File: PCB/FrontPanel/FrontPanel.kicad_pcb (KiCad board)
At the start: 2 copper layers, 130.8 x 44.5 mm, 52 parts, among them J1 Conn_01x05, J2 Conn_01x03, Q1 2N7002, Q2 2N7002, Q3 2N7002, Q4 2N7002, Q5 2N7002, SW1 SW_SPDT, SW10 RArrow, SW2 RotaryEncoder_Switch, SW3 IndepChSelect, SW4 SeriesChSelect, SW5 ParChSelect, SW6 ChAEnable, SW7 ChBEnable, SW8 ABSelect, SW9 LArrow, U1 MCU_ST_STM32G0:STM32G031F6Px, U2 CD74HC4067SM

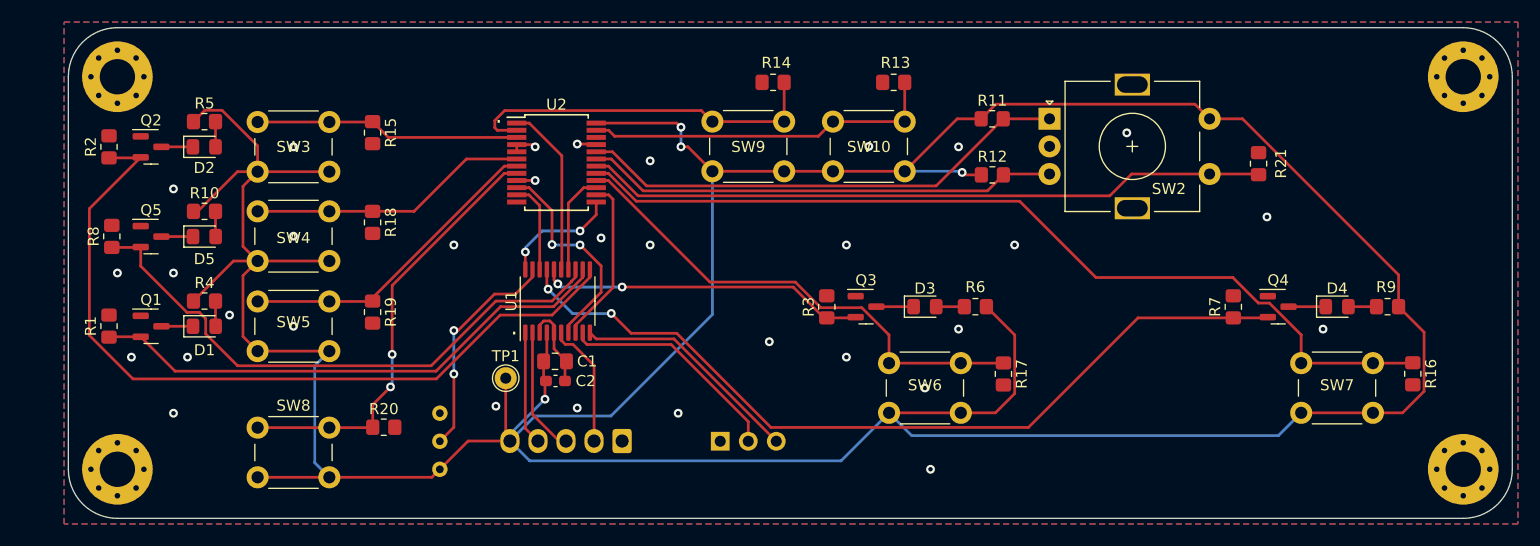
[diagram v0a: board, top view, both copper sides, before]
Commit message: Add SWD connector
USART programming is fraught with problems. It's much much
better to use SWD through an STDC14 connector.
Increased version number to v1.3
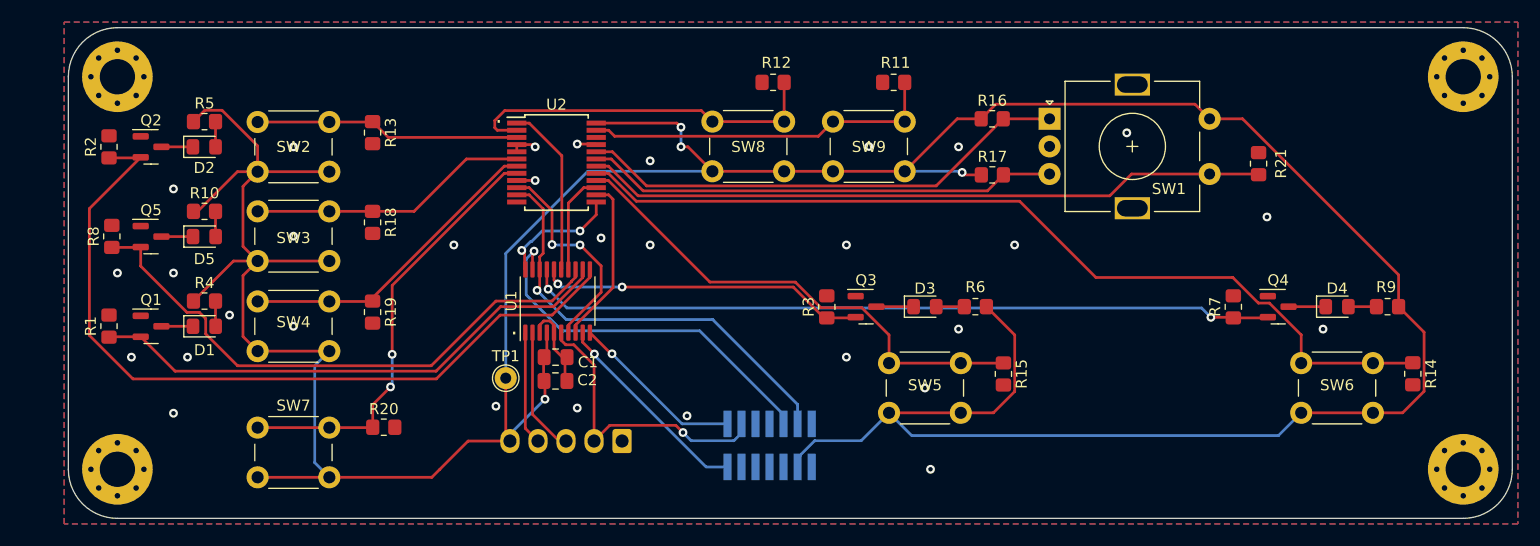
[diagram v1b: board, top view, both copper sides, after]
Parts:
- removed the SW1 at (158.8, 76.2)
- C2: footprint Capacitor_SMD:C_0603_1608Metric_Pad1.08x0.95mm_HandSolder -> Capacitor_SMD:C_0805_2012Metric_Pad1.18x1.45mm_HandSolder
- J2: value Conn_01x03 -> SWD; footprint Connector_PinHeader_2.54mm:PinHeader_1x03_P2.54mm_Vertical -> Connector_PinHeader_1.27mm:PinHeader_2x07_P1.27mm_Vertical_SMD
- moved J2 4.49 mm to (188.6, 76.6), turned to 90 degrees
- moved C1 0.38 mm to (169.2, 68.6)
- renumbered R13 to R11, R14 to R12, R15 to R13, R16 to R14, R17 to R15, R11 to R16, R12 to R17, SW2 to SW1, SW3 to SW2, SW4 to SW3, SW5 to SW4, SW6 to SW5, SW7 to SW6, SW8 to SW7, SW9 to SW8, SW10 to SW9
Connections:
- J2 pad 1: GND -> unconnected-(J2-Pad1)
- J2 pad 2: UART_TX -> unconnected-(J2-Pad2)
- J2 pad 3: UART_RX -> VCC
- U1 pad 18: S1 -> SWDIO/S1
- U1 pad 19: BOOT0 -> SWCLK
- U2 pad 11: S1 -> SWDIO/S1
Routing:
- net SWDIO/S1: track 0.00 -> 40.2 mm, vias 0 -> 1
- net SWCLK: track 0.00 -> 34.7 mm, vias 0 -> 1
- net VCC: track 364.5 -> 335.3 mm
- net BOOT0: track 20.4 -> 0.00 mm, vias 2 -> 0
- net NRESET: track 11.5 -> 27.1 mm, vias 0 -> 1
- net S1: track 8.26 -> 0.00 mm
- net CHANNEL_B_EN: track 76.4 -> 68.1 mm
- net UART_RX: track 21.0 -> 15.9 mm, vias 0 -> 1
- net UART_TX: track 20.5 -> 18.7 mm, vias 0 -> 1
- net GND: vias 32 -> 31
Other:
- board text added: "FW programming SWD interface"
- board text added: "Font del Gat Front Panel PCB v1.3 by Pau Estalella"
- board text removed: "FW programming UART interface"
- board text removed: "Font del Gat Front Panel PCB v1.2 by Pau Estalella"
- board text removed: "RX"
- board text removed: "TX"

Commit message: Give names to all networks a name
Add network labels to networks that didn't yet have a name.
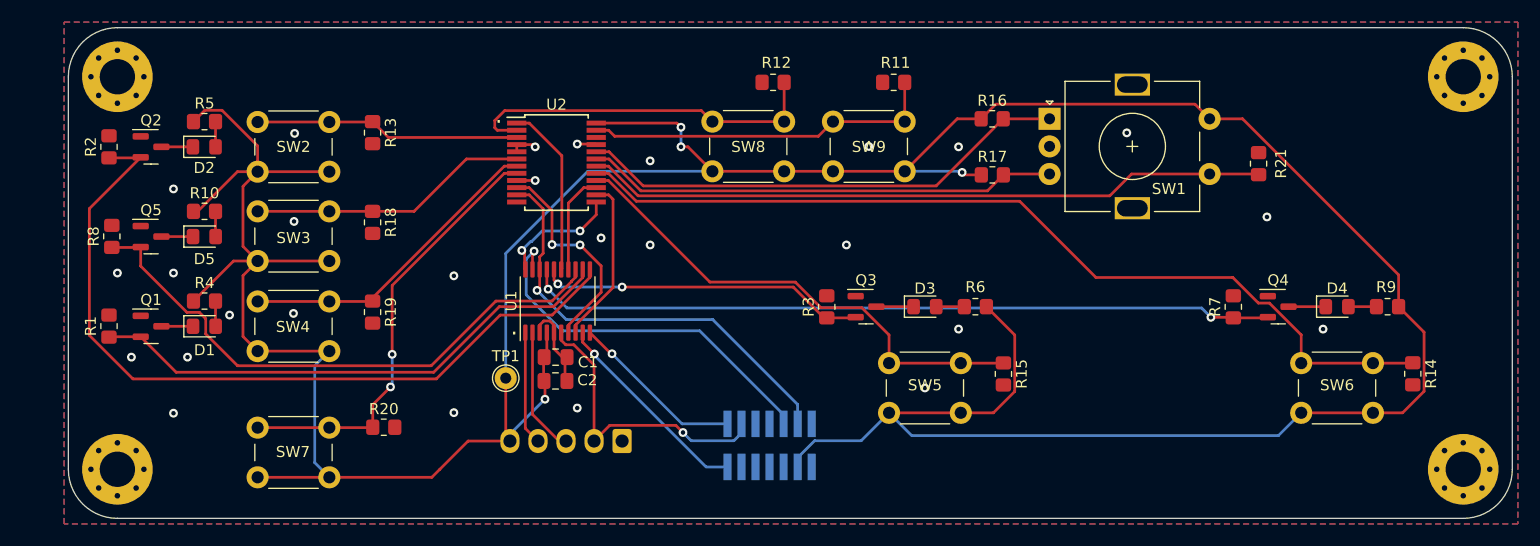
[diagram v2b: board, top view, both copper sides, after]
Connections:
- net Net-(R11-Pad1) renamed /RArrowSw
- net Net-(R12-Pad1) renamed /LArrowSw
- net Net-(R13-Pad1) renamed /IndepSelectSw
- net Net-(R14-Pad1) renamed /ChBEnableSw
- net Net-(R15-Pad1) renamed /ChAEnableSw
- net Net-(R18-Pad1) renamed /SeriesSelectSw
- net Net-(R19-Pad1) renamed /ParSelectSw
- net Net-(R20-Pad1) renamed /ABSelectSw
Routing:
- net GND: vias 31 -> 27
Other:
- board text removed: "BOOTP"
- board text removed: "USER"

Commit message: Fix 2N7002 footprint
The footprint for the 2N7002 MOSFETs was taken from the one
of a 2N7000, which has the gate and the source pins exchanged.
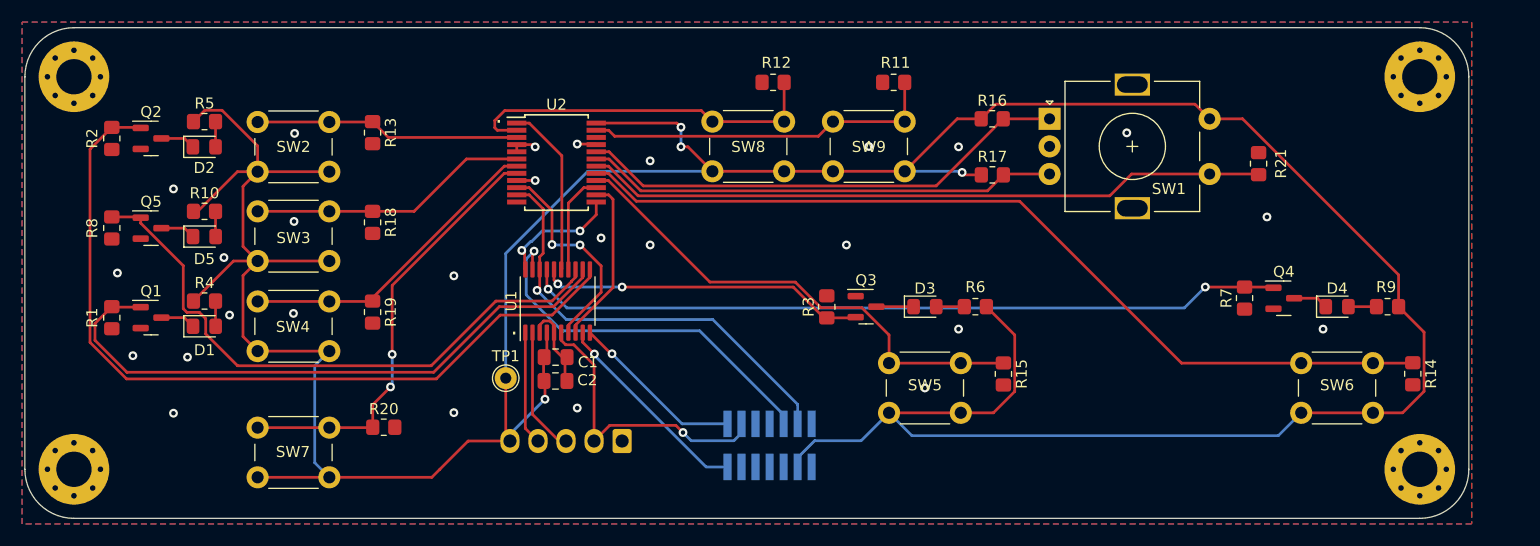
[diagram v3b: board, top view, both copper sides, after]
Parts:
- moved H2 3.94 mm to (247.5, 43.2)
- moved H4 3.94 mm to (247.5, 78.7)
- moved H1 3.94 mm to (125.6, 78.7)
- moved H3 3.94 mm to (125.6, 43.2)
- moved R7 1.29 mm to (231.6, 63.2), turned to -90 degrees
- moved Q4 0.92 mm to (235.2, 63.2)
- moved R1 0.80 mm to (129.0, 65.0), turned to -90 degrees
- moved R2 0.80 mm to (129.0, 48.8), turned to -90 degrees
- moved Q1 0.79 mm to (132.6, 65.0)
- moved Q2 0.76 mm to (132.6, 48.8)
- moved Q5 0.76 mm to (132.6, 56.9)
- moved R8 0.76 mm to (129.0, 56.9), turned to -90 degrees
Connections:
- Q1 pad 1: GND -> PAR_CHANNEL_EN
- Q1 pad 2: PAR_CHANNEL_EN -> GND
- Q2 pad 1: GND -> INDEP_CHANNEL_EN
- Q2 pad 2: INDEP_CHANNEL_EN -> GND
- Q4 pad 1: GND -> CHANNEL_B_EN
- Q4 pad 2: CHANNEL_B_EN -> GND
- Q5 pad 1: GND -> SERIES_CHANNEL_EN
- Q5 pad 2: SERIES_CHANNEL_EN -> GND
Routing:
- net PAR_CHANNEL_EN: track 48.5 -> 56.0 mm
- net SERIES_CHANNEL_EN: track 52.3 -> 55.0 mm
- net INDEP_CHANNEL_EN: track 72.4 -> 74.1 mm
- net /ChBEnableSw: track 82.6 -> 81.1 mm
- net CHANNEL_B_EN: track 68.1 -> 69.1 mm
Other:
- board text added: "Font del Gat Front Panel PCB v1.4 by Pau Estalella"
- board text removed: "Font del Gat Front Panel PCB v1.3 by Pau Estalella"

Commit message: Fixes for the front panel
Add a 3V3 regulator to convert the 5V input.
Fix RX/TX mix-up
Fix footprint for one last 2N7002 mosfet
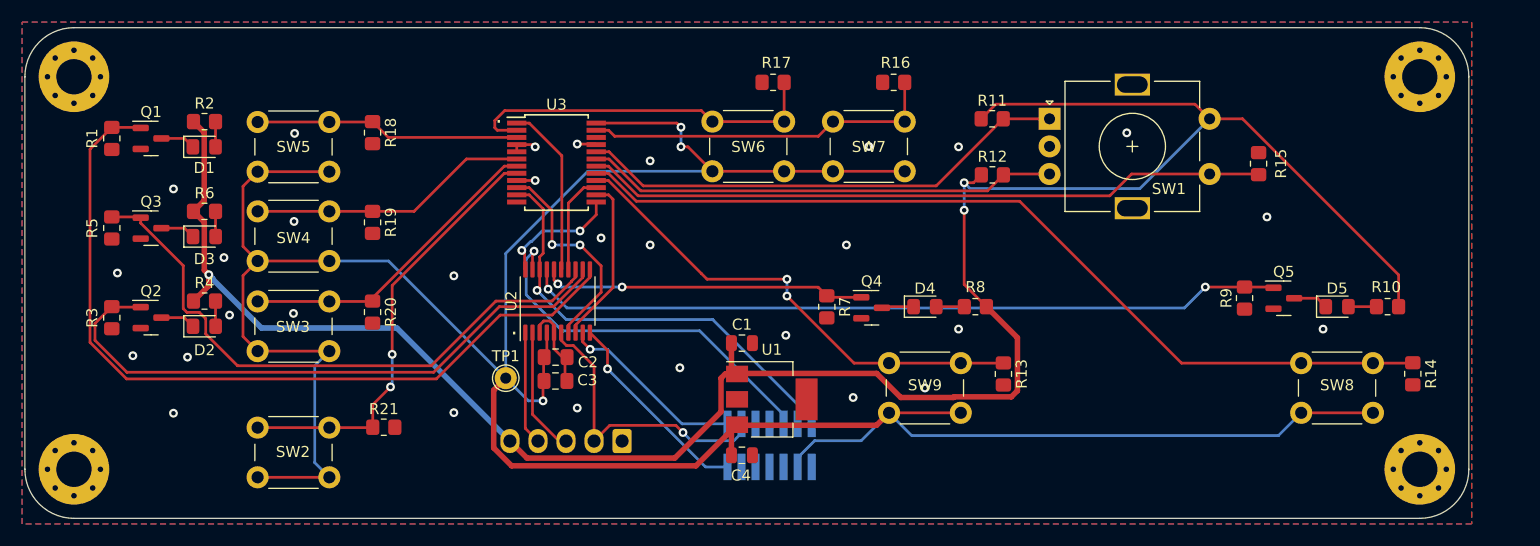
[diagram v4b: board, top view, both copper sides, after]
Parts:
- removed the Q3 at (197.4, 64.0)
- added C1: 1uF, Capacitor_SMD:C_0805_2012Metric, F.Cu at (186.1, 67.3)
- added C4: 1uF, Capacitor_SMD:C_0805_2012Metric, F.Cu at (186.1, 77.5)
- added Q4: 2N7002, Package_TO_SOT_SMD:SOT-23, F.Cu at (197.9, 64.1)
- added U1: MCP1703A-3302_SOT223, Package_TO_SOT_SMD:SOT-223-3_TabPin2, F.Cu at (188.8, 72.4)
- turned R7 to -90 degrees
- renumbered C1 to C2, C2 to C3, D2 to D1, D1 to D2, D5 to D3, D3 to D4, D4 to D5, Q2 to Q1, Q1 to Q2, Q5 to Q3, Q4 to Q5, R2 to R1, R9 to R10, R16 to R11, R17 to R12, R15 to R13, R21 to R15, R11 to R16, R12 to R17, R13 to R18, R18 to R19, R5 to R2, R19 to R20, R20 to R21, R1 to R3, R8 to R5, R10 to R6, R3 to R7, R6 to R8, R7 to R9, SW7 to SW2, SW4 to SW3, SW3 to SW4, SW2 to SW5, SW8 to SW6, SW9 to SW7, SW6 to SW8, SW5 to SW9, U1 to U2, U2 to U3
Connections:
- C2 pad 1: VCC -> +3V3
- C3 pad 1: VCC -> +3V3
- J2 pad 13: UART_TX -> UART_RX
- J2 pad 14: UART_RX -> UART_TX
- J2 pad 3: VCC -> +3V3
- SW2 pad 2: VCC -> +3V3
- SW3 pad 2: VCC -> +3V3
- SW4 pad 2: VCC -> +3V3
- SW5 pad 2: VCC -> +3V3
- SW6 pad 2: VCC -> +3V3
- SW7 pad 2: VCC -> +3V3
- SW8 pad 2: VCC -> +3V3
- SW9 pad 2: VCC -> +3V3
- TP1 pad 1: VCC -> +3V3
- U2 pad 4: VCC -> +3V3
- U3 pad 24: VCC -> +3V3
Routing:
- net +3V3: track 0.00 -> 263.1 mm, vias 0 -> 3
- net VCC: track 335.3 -> 202.9 mm, vias 4 -> 3
- net UART_RX: track 15.9 -> 18.5 mm
- net UART_TX: track 18.7 -> 17.0 mm
- net /ChAEnableSw: track 45.2 -> 44.6 mm, vias 0 -> 2
- net GND: vias 27 -> 30
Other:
- board text added: "Font del Gat Front Panel PCB v1.5 by Pau Estalella"
- board text removed: "Font del Gat Front Panel PCB v1.4 by Pau Estalella"
